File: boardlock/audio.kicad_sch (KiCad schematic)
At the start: 10 parts, among them J3 Micro_SD_Card_Det1, U7 MAX98357AETE+T

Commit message: lab updates
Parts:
- removed C15, C17: 10uF, symbol Device:C
- removed C16: 1uF, symbol Device:C
- removed U8: ~, boardlock:SOT23-6, symbol custom_library:AP3602
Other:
- note added: "Digital Audio Amplifier"
- note removed: "5V Charge Pump"
- note removed: "Buzzer Power Boost Charge Pump"
- note removed: "Dgital Audio Amplifier"
- note removed: "Keeping Charge Pump Here Just in Case we need to use it. Unlikley with the boost converter present."
- note removed: "Need to add connector/pads for buzzer to solder onto"

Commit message: not sure what I changed
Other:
- note added: "TODO: ADD BUZZER DRIVER CIRCUIT"
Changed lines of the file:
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@@
     (effects (font (size 1.27 1.27)) (justify right bottom))
+  )
+  (text "TODO: ADD BUZZER DRIVER CIRCUIT" (at 185.42 90.17 0)
+    (effects (font (size 2.5 2.5) (thickness 0.5) bold) (justify left bottom))
   )
   (text "Digital Audio Amplifier" (at 60.96 25.4 0)

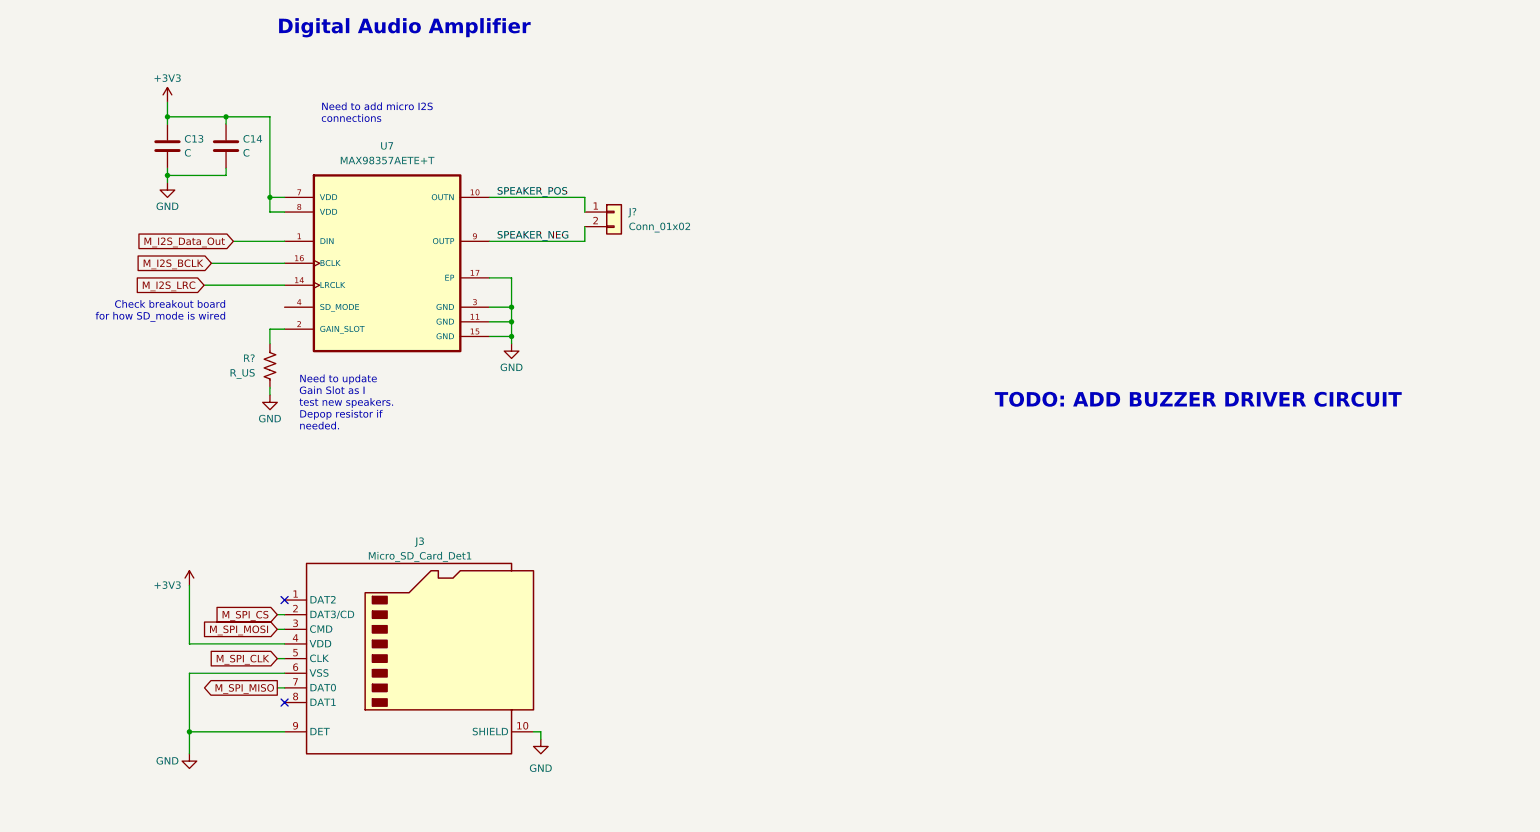
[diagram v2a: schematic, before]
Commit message: added footprints and an LPF to audio
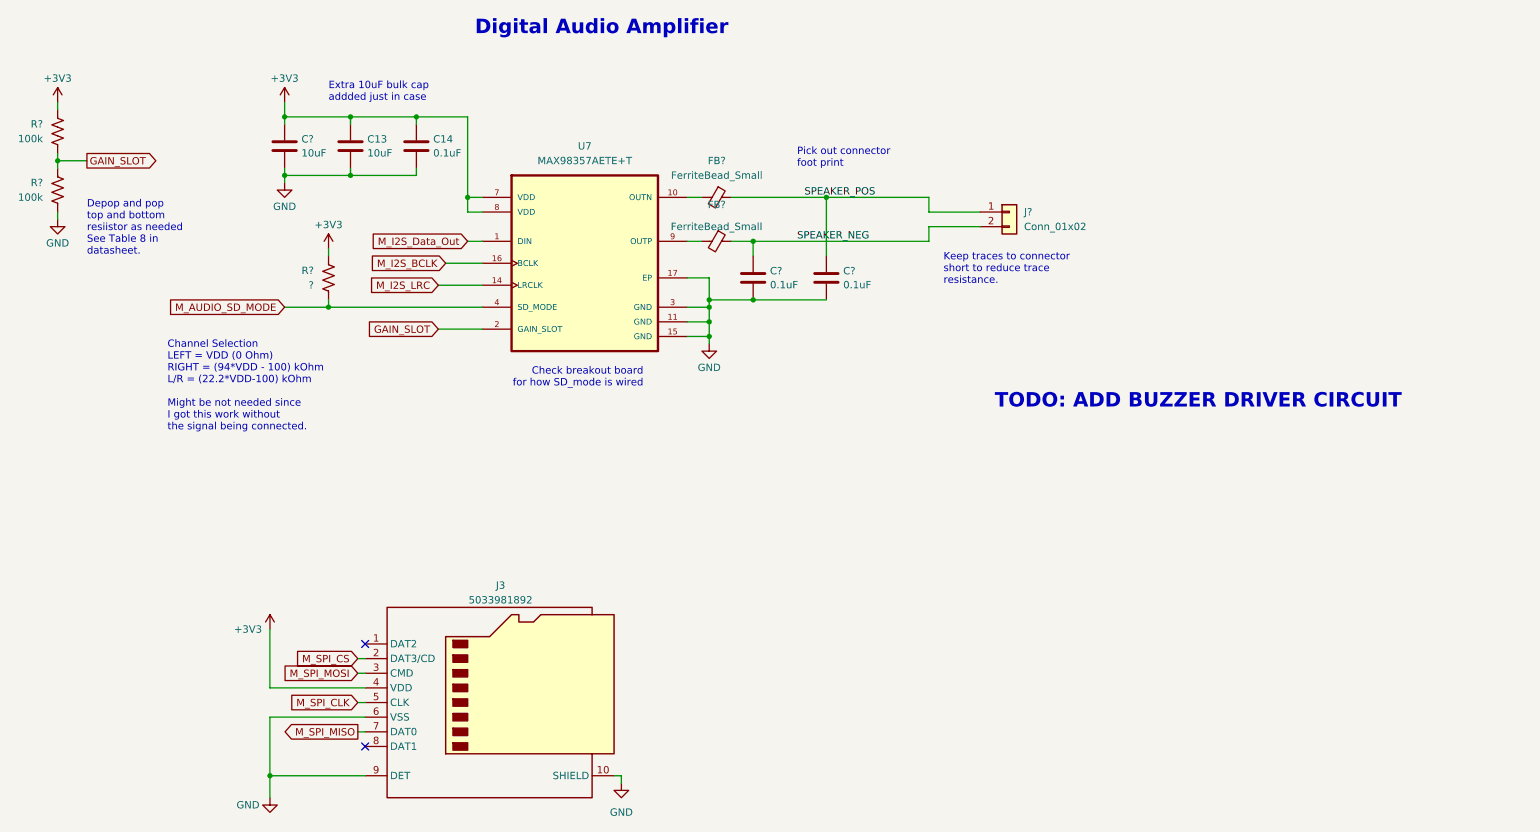
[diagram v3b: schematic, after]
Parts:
- added C? (x2): 0.1uF, Capacitor_SMD:C_0603_1608Metric_Pad1.08x0.95mm_HandSolder, symbol Device:C
- added C?: 10uF, Capacitor_SMD:C_0805_2012Metric_Pad1.18x1.45mm_HandSolder, symbol Device:C
- added FB? (x2): FerriteBead_Small, symbol Device:FerriteBead_Small
- added R?: ?, Resistor_SMD:R_0805_2012Metric_Pad1.20x1.40mm_HandSolder, symbol Device:R_US
- added R?: 100k, Resistor_SMD:R_0805_2012Metric_Pad1.20x1.40mm_HandSolder, symbol Device:R_US
- C13: value C -> 10uF; footprint (none) -> Capacitor_SMD:C_0805_2012Metric_Pad1.18x1.45mm_HandSolder
- C14: value C -> 0.1uF; footprint (none) -> Capacitor_SMD:C_0603_1608Metric_Pad1.08x0.95mm_HandSolder
- J3: value Micro_SD_Card_Det1 -> 5033981892; footprint (none) -> microSD 503398-1892:MOLEX_503398-1892
- R?: value R_US -> 100k; footprint (none) -> Resistor_SMD:R_0805_2012Metric_Pad1.20x1.40mm_HandSolder
- U7: Availability In Stock -> (none); Check_prices https://www.snapeda.com/parts/MAX98357AETE+T/Analog+Devices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 -> (none); Price None -> (none); Purchase-URL https://www.snapeda.com/api/url_track_click_mouser/?unipart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 -> (none); SnapEDA_Link https://www.snapeda.com/parts/MAX98357AETE+T/Analog+Devices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 -> (none)
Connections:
- net +3V3: now also C?.1, R?.1, R?.1
- net GND: now also C?.2, C?.2, C?.2
- net SPEAKER_NEG: now also C?.1, FB?.1; no longer U7.9 (OUTP)
- net SPEAKER_POS: now also C?.1, FB?.1; no longer U7.10 (OUTN)
- net GAIN_SLOT: now reaches R?.1, U7.2 (GAIN_SLOT)
- net GAIN_SLOT: now also R?.2
- net M_AUDIO_SD_MODE: now reaches U7.4 (SD_MODE)
- net M_AUDIO_SD_MODE: now also R?.2
- new net: FB?.2, U7.10 (OUTN)
- new net: FB?.2, U7.9 (OUTP)
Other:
- note added: "Channel Selection LEFT = VDD (0 Ohm) RIGHT = (94*VDD - 100) kOhm L/R = (22.2*VDD-100) kOhm Might be not needed since I got this work without the signal being connected."
- note added: "Depop and pop top and bottom resiistor as needed See Table 8 in datasheet."
- note added: "Extra 10uF bulk cap addded just in case"
- note added: "Keep traces to connector short to reduce trace resistance."
- note added: "Pick out connector foot print"
- note removed: "Need to add micro I2S connections"
- note removed: "Need to update Gain Slot as I test new speakers. Depop resistor if needed."
- moved on the sheet: C13, C14, J3, J?, R?, U7

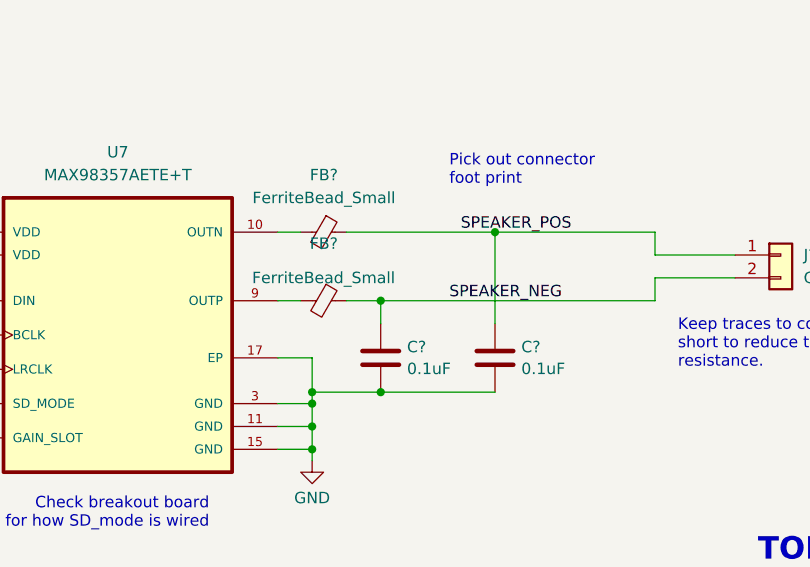
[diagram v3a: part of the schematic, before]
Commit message: continuing to add footprints
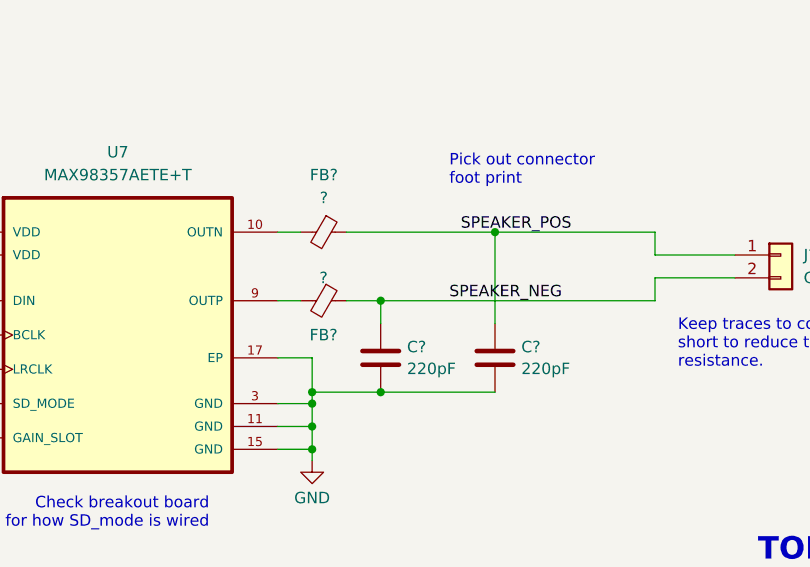
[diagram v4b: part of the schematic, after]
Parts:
- C?: value 0.1uF -> 220pF
- C?: value 0.1uF -> 220pF; footprint Capacitor_SMD:C_0603_1608Metric_Pad1.08x0.95mm_HandSolder -> Capacitor_SMD:C_0805_2012Metric_Pad1.18x1.45mm_HandSolder
- FB? (x2): value FerriteBead_Small -> ?; footprint (none) -> Inductor_SMD:L_0805_2012Metric_Pad1.15x1.40mm_HandSolder
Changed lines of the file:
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@@
       (effects (font (size 1.27 1.27)) (justify left))
     )
-    (property "Value" "0.1uF" (at 146.431 68.5221 0)
+    (property "Value" "220pF" (at 146.431 68.5221 0)
       (effects (font (size 1.27 1.27)) (justify left))
     )
@@
       (effects (font (size 1.27 1.27)))
     )
-    (property "Value" "FerriteBead_Small" (at 137.1981 49.53 90)
-      (effects (font (size 1.27 1.27)))
-    )
-    (property "Footprint" "" (at 137.16 51.562 90)
+    (property "Value" "?" (at 137.1981 49.53 90)
+      (effects (font (size 1.27 1.27)))
+    )
+    (property "Footprint" "Inductor_SMD:L_0805_2012Metric_Pad1.15x1.40mm_HandSolder" (at 137.16 51.562 90)
       (effects (font (size 1.27 1.27)) hide)
     )
@@
   (symbol (lib_id "Device:FerriteBead_Small") (at 137.16 60.96 270) (unit 1)
     (in_bom yes) (on_board yes) (dnp no)
-    (property "Reference" "FB?" (at 137.1981 54.61 90)
-      (effects (font (size 1.27 1.27)))
-    )
-    (property "Value" "FerriteBead_Small" (at 137.16 58.42 90)
-      (effects (font (size 1.27 1.27)))
-    )
-    (property "Footprint" "" (at 137.16 59.182 90)
+    (property "Reference" "FB?" (at 137.16 64.77 90)
+      (effects (font (size 1.27 1.27)))
+    )
+    (property "Value" "?" (at 137.16 58.42 90)
+      (effects (font (size 1.27 1.27)))
+    )
+    (property "Footprint" "Inductor_SMD:L_0805_2012Metric_Pad1.15x1.40mm_HandSolder" (at 137.16 59.182 90)
       (effects (font (size 1.27 1.27)) hide)
     )
@@
       (effects (font (size 1.27 1.27)) (justify left))
     )
-    (property "Value" "0.1uF" (at 159.131 68.5221 0)
-      (effects (font (size 1.27 1.27)) (justify left))
-    )
-    (property "Footprint" "Capacitor_SMD:C_0603_1608Metric_Pad1.08x0.95mm_HandSolder" (at 157.1752 71.12 0)
-      (effects (font (size 1.27 1.27)) hide)
-    )
+    (property "Value" "220pF" (at 159.131 68.5221 0)
+      (effects (font (size 1.27 1.27)) (justify left))
+    )
+    (property "Footprint" "Capacitor_SMD:C_0805_2012Metric_Pad1.18x1.45mm_HandSolder" (at 157.1752 71.12 0)
+      (effects (font (size 1.27 1.27)) hide)
+    )

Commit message: more footprint selection
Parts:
- added C?: 47n, Capacitor_SMD:C_0805_2012Metric_Pad1.18x1.45mm_HandSolder, symbol Device:C
- C?: value 220pF -> 47n; footprint Capacitor_SMD:C_0603_1608Metric_Pad1.08x0.95mm_HandSolder -> Capacitor_SMD:C_0805_2012Metric_Pad1.18x1.45mm_HandSolder
- C?: value 220pF -> 47n
- FB? (x2): value ? -> 4.7uH; footprint Inductor_SMD:L_0805_2012Metric_Pad1.15x1.40mm_HandSolder -> Inductor_SMD:L_1210_3225Metric_Pad1.42x2.65mm_HandSolder
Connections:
- net SPEAKER_NEG: now also C?.2
- net SPEAKER_POS: now also C?.1
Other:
- note added: "Output fillter to elim switching noise. R = 4 Ohm -3dB @ 70kHz R = 8 Ohm -3dB @ 160kHz"
- note removed: "Pick out connector foot print"
- moved on the sheet: C?, FB?, J?

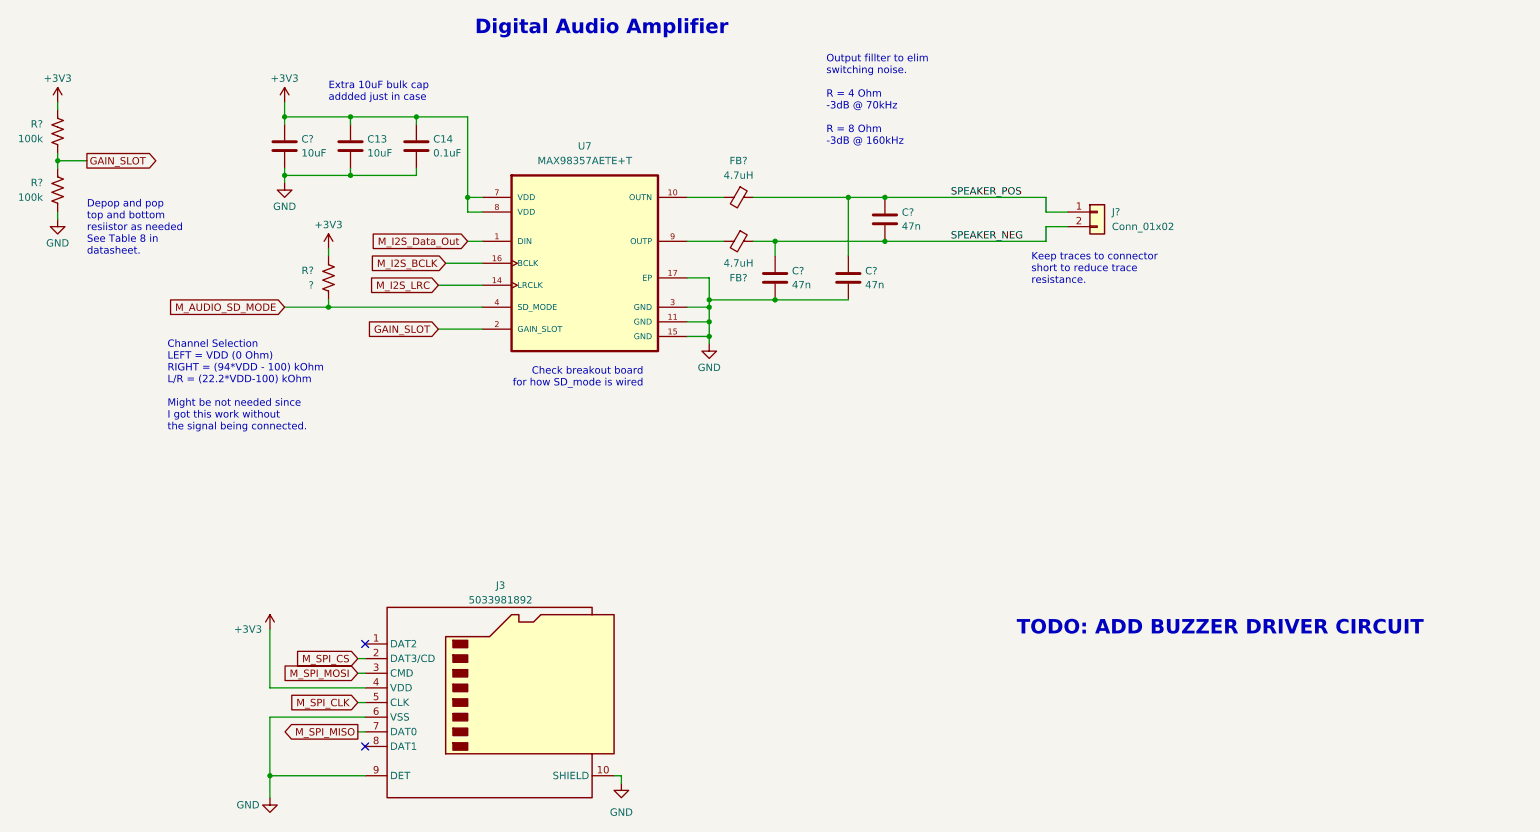
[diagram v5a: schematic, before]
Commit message: added buzzer power circuit
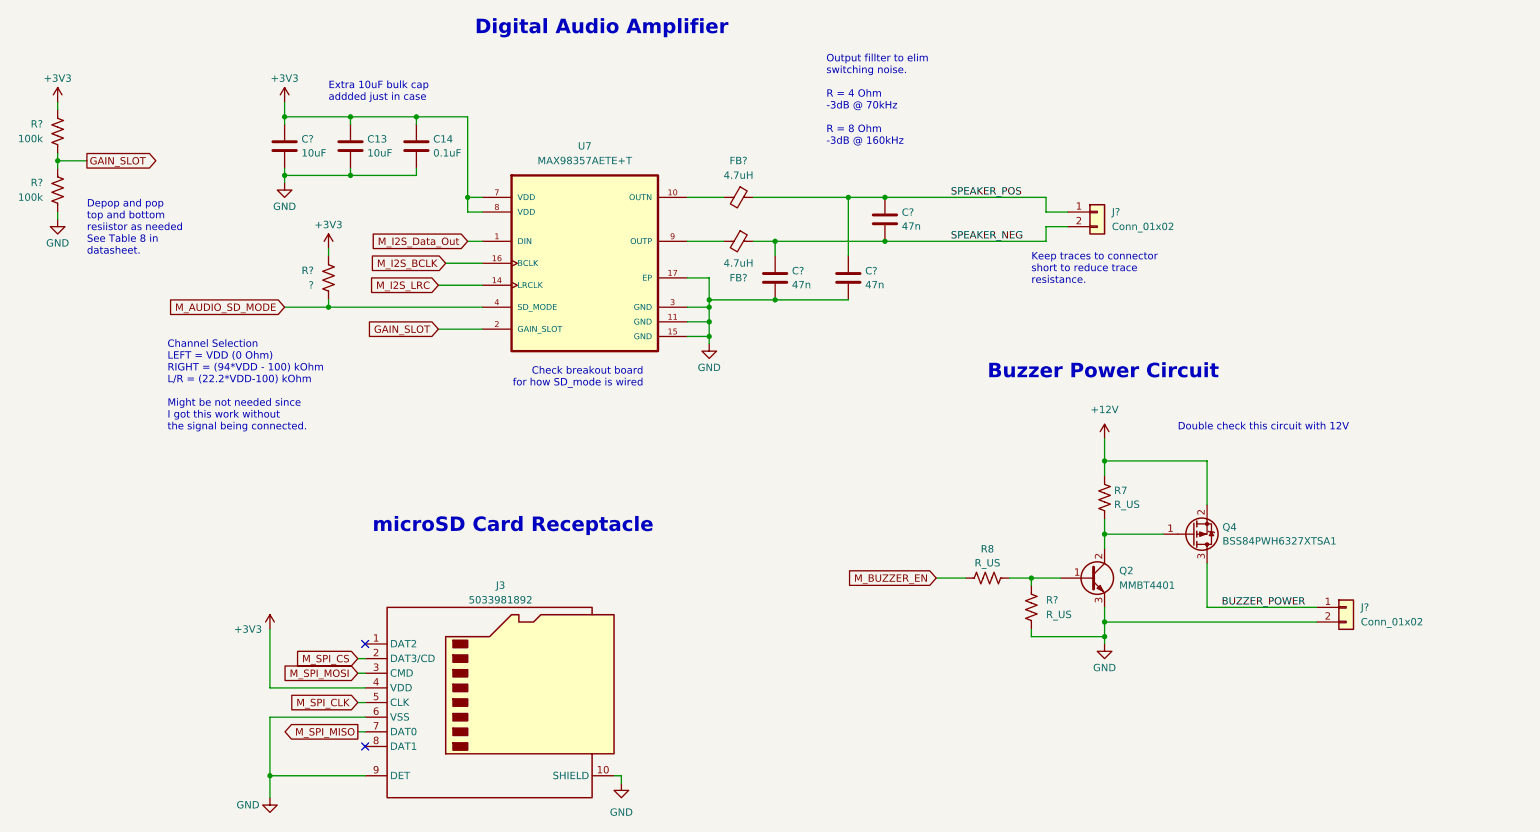
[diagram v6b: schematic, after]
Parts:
- added J?: Conn_01x02, Connector_JST:JST_XA_B02B-XASK-1-A_1x02_P2.50mm_Vertical, symbol Connector_Generic:Conn_01x02
- added Q2: MMBT4401, symbol Device:Q_NPN_BCE
- added Q4: BSS84PWH6327XTSA1, Package_TO_SOT_SMD:SOT-323_SC-70_Handsoldering, symbol Device:Q_PMOS_GSD
- added R7, R8, R?: R_US, symbol Device:R_US
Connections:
- net GND: now also J?.2 (Pin_2), Q2.3 (E), R?.2
- new net: Q2.2 (C), Q4.1 (G), R7.2
- new net: Q2.1 (B), R8.2, R?.1
- new net +12V: Q4.2 (S), R7.1
- new net BUZZER_POWER: J?.1 (Pin_1), Q4.3 (D)
- new net M_BUZZER_EN: R8.1
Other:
- note added: "Buzzer Power Circuit"
- note added: "Double check this circuit with 12V"
- note added: "microSD Card Receptacle"
- note removed: "TODO: ADD BUZZER DRIVER CIRCUIT"
